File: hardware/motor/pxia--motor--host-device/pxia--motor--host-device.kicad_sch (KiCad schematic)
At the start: 5 parts

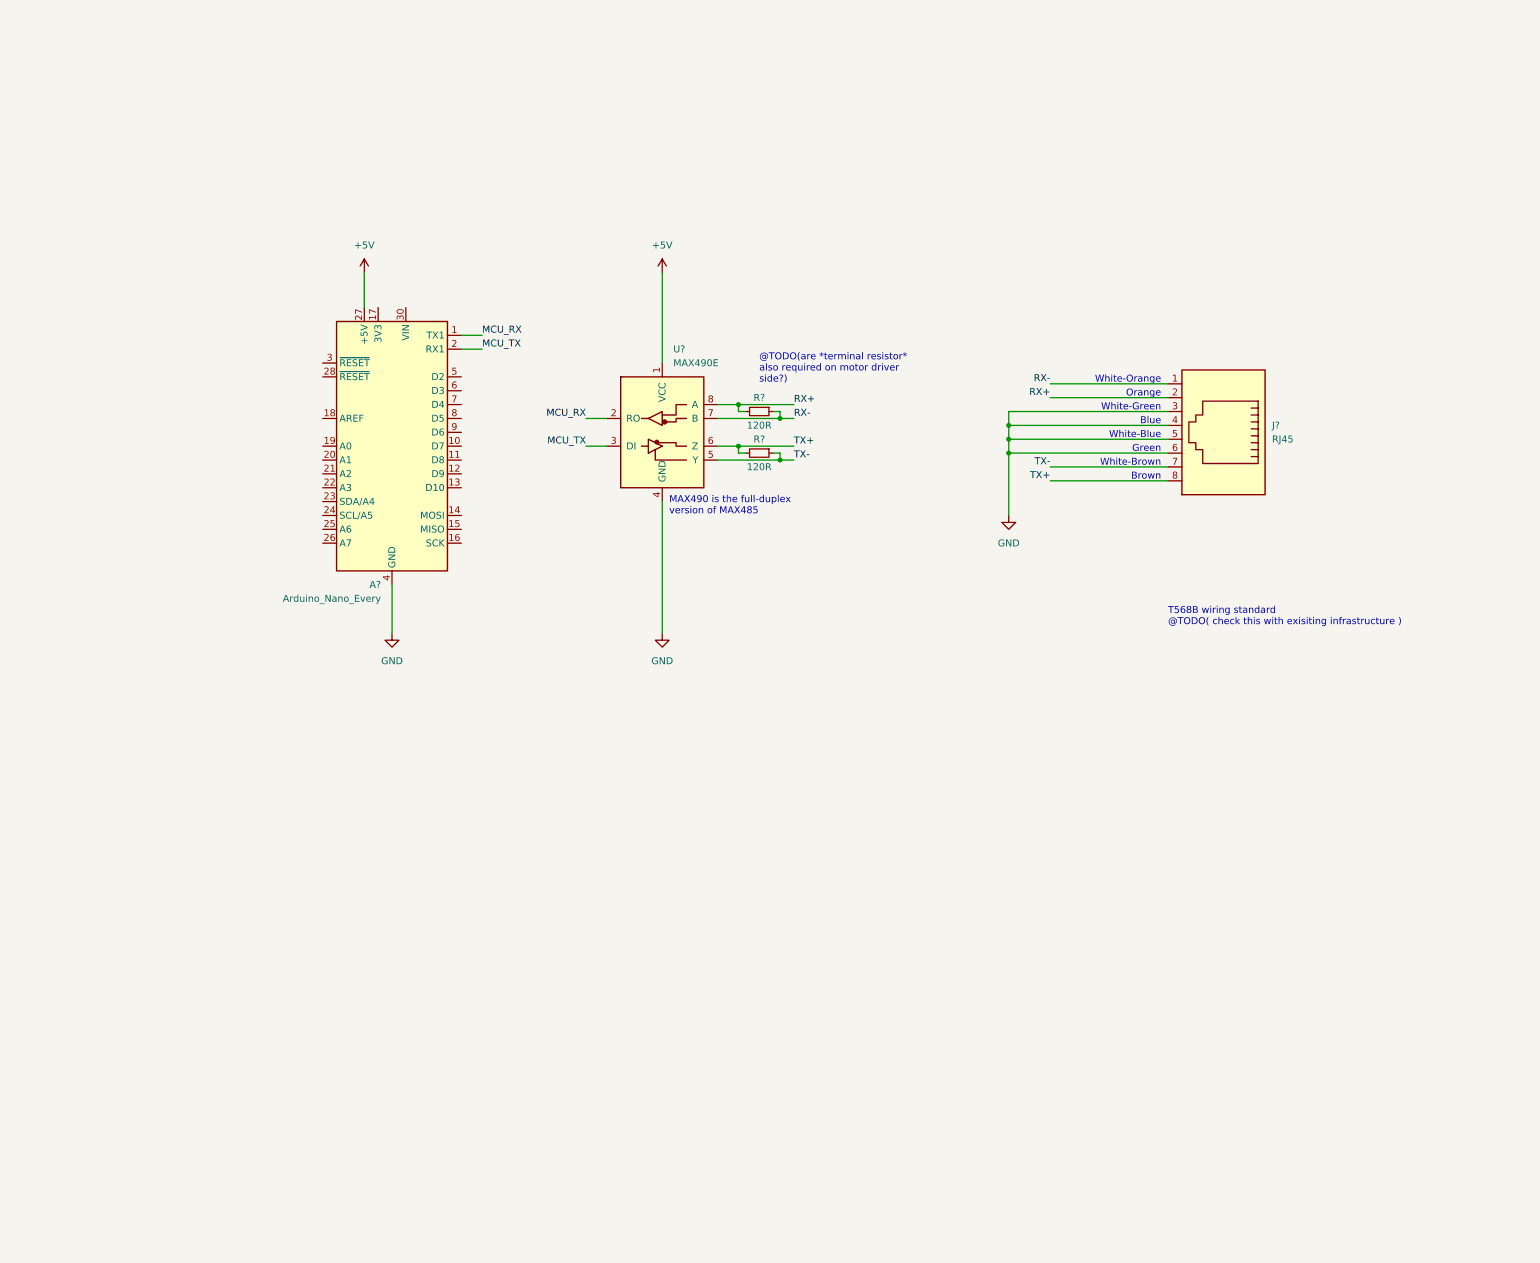
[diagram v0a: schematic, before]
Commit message: updated schematics + footprint
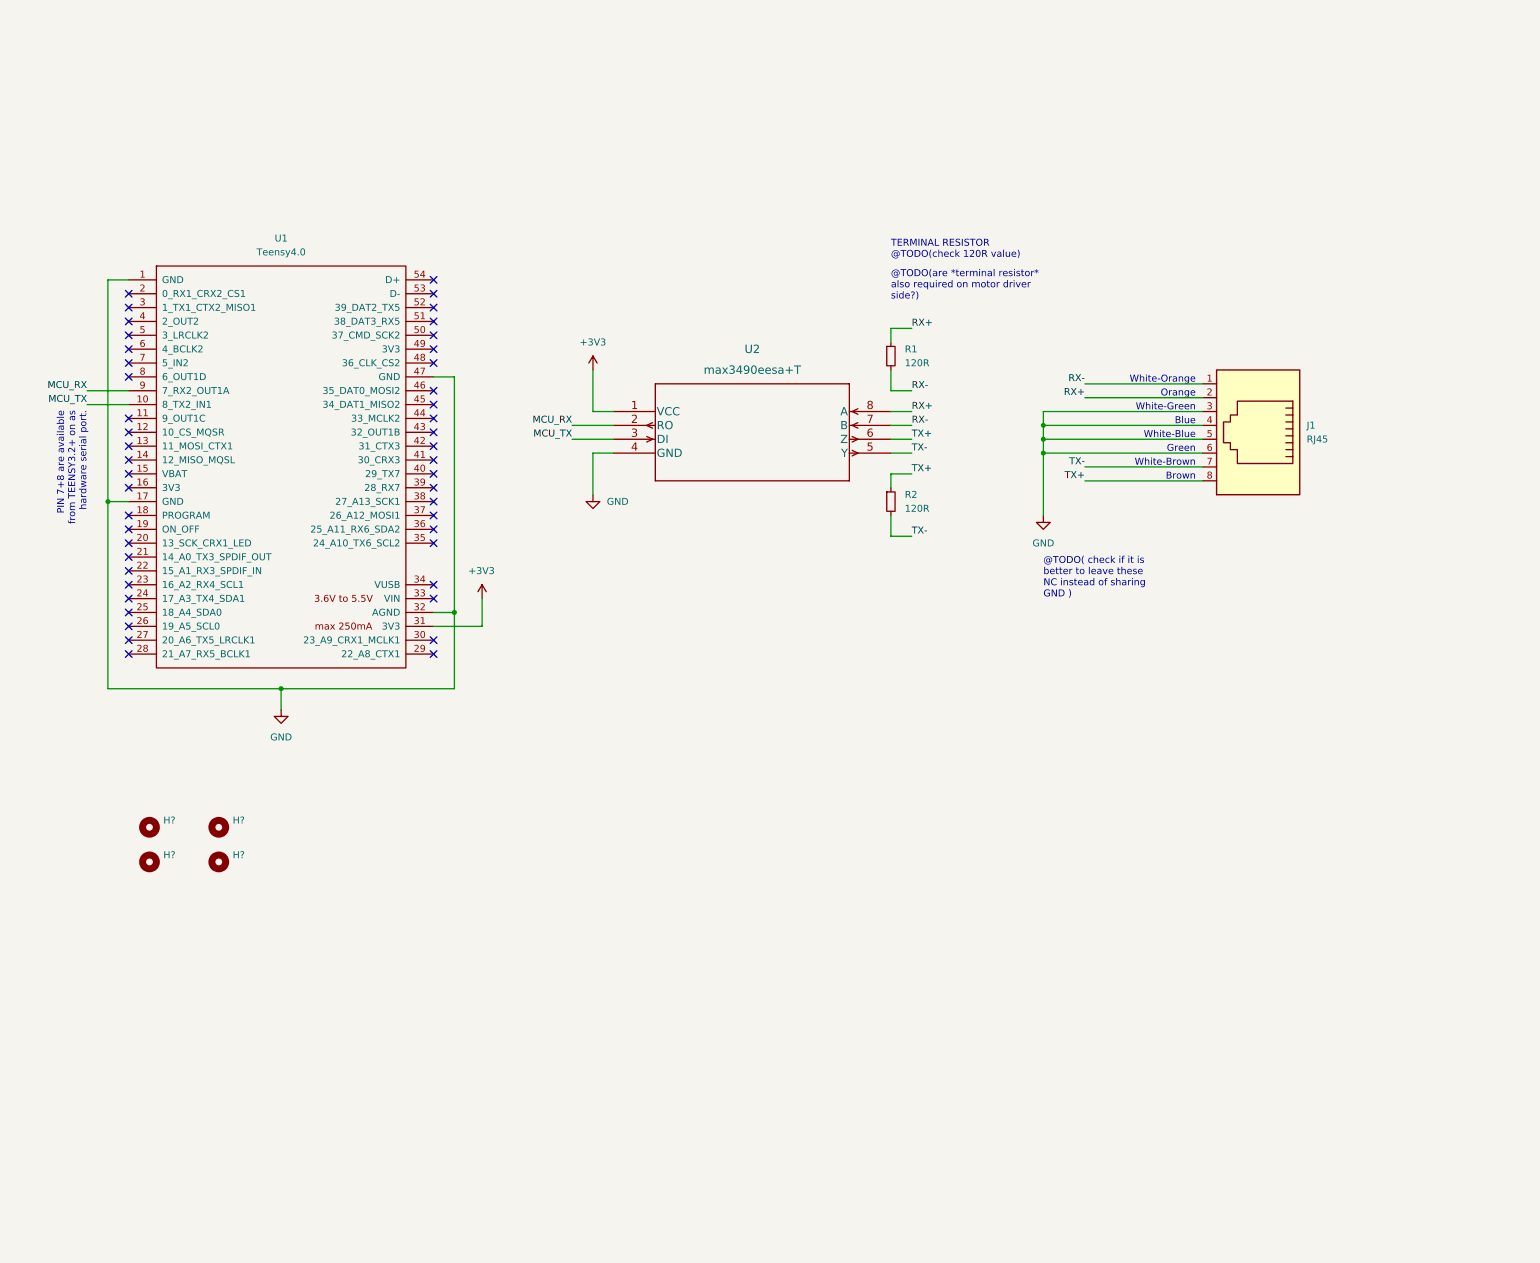
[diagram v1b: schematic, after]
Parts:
- removed A?: Arduino_Nano_Every, Module:Arduino_Nano, symbol MCU_Module:Arduino_Nano_Every
- removed R? (x2): 120R, symbol Device:R_Small
- removed U?: MAX490E, symbol Interface_UART:MAX490E
- added H? (x4): (no value), symbol Mechanical:MountingHole
- added R1, R2: 120R, Resistor_SMD:R_0805_2012Metric_Pad1.20x1.40mm_HandSolder, symbol Device:R_Small
- added U1: Teensy4.0, TEENSY:Teensy40, symbol teensy:Teensy4.0
- added U2: max3490eesa+T, Package_SO:SOIC-8_3.9x4.9mm_P1.27mm, symbol MAX3490EESA+T:max3490eesa+T
- J1: renamed from J?; footprint (none) -> Connector_RJ:RJ45_OST_PJ012-8P8CX_Vertical
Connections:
- net GND: now also U1.1 (GND), U1.17 (GND), U1.32 (AGND), U1.47 (GND), U2.4 (GND)
- net MCU_RX: now also U1.9 (7_RX2_OUT1A), U2.2 (RO)
- net MCU_TX: now also U1.10 (8_TX2_IN1), U2.3 (DI)
- net RX+: now also R1.1, U2.8 (A)
- net RX-: now also R1.2, U2.7 (B)
- net TX+: now also R2.1, U2.6 (Z)
- net TX-: now also R2.2, U2.5 (Y)
- new net +3V3: U1.31 (3V3), U2.1 (VCC)
- no-connect marks 0 -> 47
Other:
- note added: "@TODO( check if it is better to leave these NC instead of sharing GND )"
- note added: "PIN 7+8 are available from TEENSY3.2+ on as hardware serial port."
- note added: "TERMINAL RESISTOR @TODO(check 120R value)"
- note removed: "MAX490 is the full-duplex version of MAX485"
- note removed: "T568B wiring standard @TODO( check this with exisiting infrastructure )"
- moved on the sheet: J1

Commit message: added drawing, added ESP32 to host board
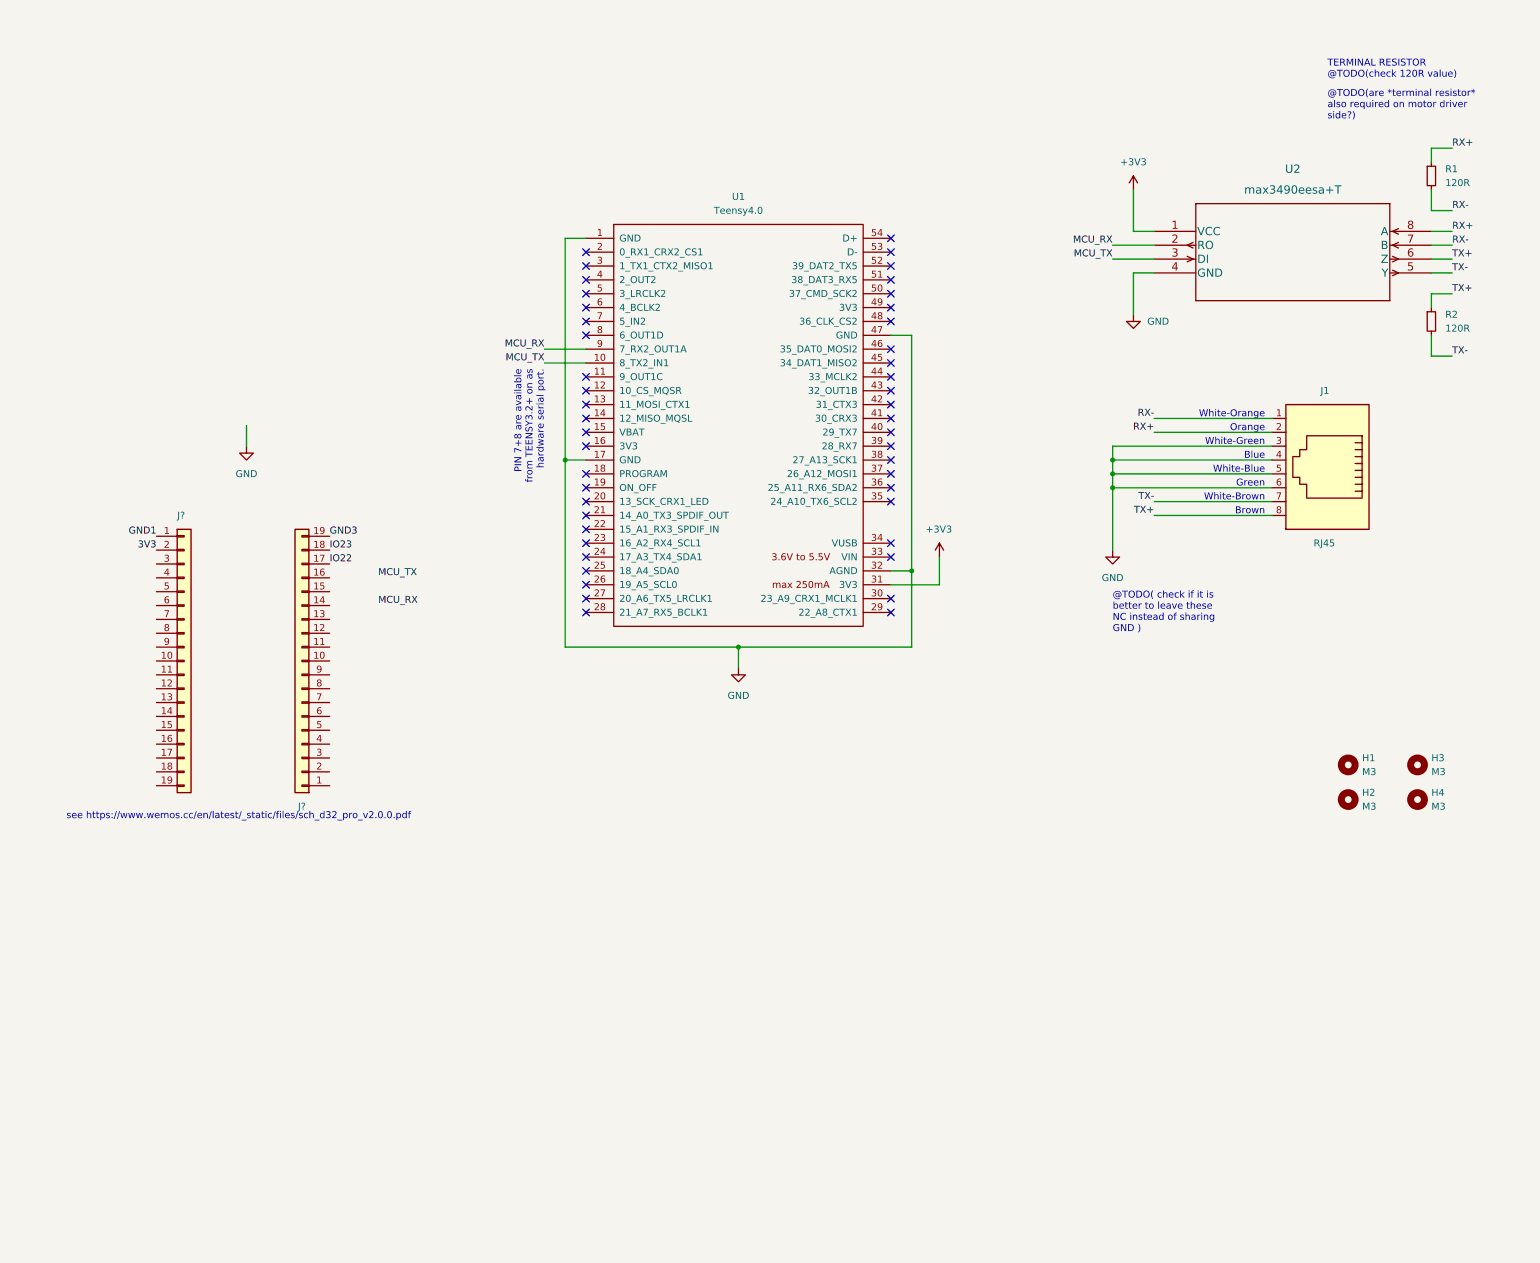
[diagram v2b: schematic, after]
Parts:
- added J? (x2): (no value), symbol Connector_Generic:Conn_01x19
- H1, H2, H3, H4: renamed from H?; value (none) -> M3; footprint (none) -> MountingHole:MountingHole_3.2mm_M3
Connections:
- new net 3V3: J?.2 (Pin_2)
- new net GND1: J?.1 (Pin_1)
- new net GND3: J?.19 (Pin_19)
- new net IO22: J?.17 (Pin_17)
- new net IO23: J?.18 (Pin_18)
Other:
- note added: "see https://www.wemos.cc/en/latest/_static/files/sch_d32_pro_v2.0.0.pdf"
- moved on the sheet: H1, H2, H3, H4, J1, R1, R2, U1, U2

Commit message: finished schematics and most of pcb layout
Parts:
- removed J? (x2): (no value), symbol Connector_Generic:Conn_01x19
- added J2: Lolin D32 Pro 2.0.0 (ESP32) PIN01–16, Connector_PinSocket_2.54mm:PinSocket_1x16_P2.54mm_Vertical, symbol Connector_Generic:Conn_01x16
- added J3: GENERIC_UART, Connector_Molex:Molex_Nano-Fit_105313-xx04_1x04_P2.50mm_Horizontal, symbol Connector_Generic:Conn_01x04
- added J4: Lolin D32 Pro 2.0.0 (ESP32) PIN17–32, Connector_PinSocket_2.54mm:PinSocket_1x16_P2.54mm_Vertical, symbol Connector_Generic:Conn_01x16
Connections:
- net +3V3: now also J2.1 (Pin_1), J3.1 (Pin_1)
- net GND: now also J3.4 (Pin_4), J4.1 (Pin_1), J4.16 (Pin_16); no longer J1.3, J1.4, J1.5, J1.6
- net MCU_RX renamed IO13
- net IO13: now also J2.13 (Pin_13), J3.3 (Pin_3)
- net MCU_TX renamed IO14/T-CS
- net IO14/T-CS: now also J2.11 (Pin_11), J3.2 (Pin_2)
- new net: J1.3, J1.4, J1.5, J1.6
- new net BAT: J2.16 (Pin_16)
- new net EN: J2.14 (Pin_14)
- new net IO00: J4.13 (Pin_13)
- new net IO02: J4.14 (Pin_14)
- new net IO04/TF-CS: J4.12 (Pin_12)
- new net IO05/SS: J4.9 (Pin_9)
- new net IO12/TS-CS: J2.12 (Pin_12)
- new net IO15: J4.15 (Pin_15)
- new net IO18/SCK: J4.8 (Pin_8)
- new net IO19/MISO: J4.7 (Pin_7)
- new net IO21/SDA: J4.6 (Pin_6)
- new net IO22/SCL: J4.3 (Pin_3)
- new net IO23/MOSI: J4.2 (Pin_2)
- new net IO25/DAC1: J2.8 (Pin_8)
- new net IO26/DAC2: J2.9 (Pin_9)
- new net IO27/T-DC: J2.10 (Pin_10)
- new net IO32/A/T-LED: J2.6 (Pin_6)
- new net IO33/A/T-RST: J2.7 (Pin_7)
- new net IO34/A: J2.5 (Pin_5)
- new net NC: J4.10 (Pin_10), J4.11 (Pin_11)
- new net RESET: J2.2 (Pin_2)
- new net RXD0: J4.5 (Pin_5)
- new net TXD0: J4.4 (Pin_4)
- new net USB: J2.15 (Pin_15)
- new net VN: J2.4 (Pin_4)
- new net VP: J2.3 (Pin_3)
- no-connect marks 47 -> 73
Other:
- note added: "@add https://shop.pimoroni.com/products/feathers3-esp32-s3?variant=39762596298835"
- note added: "@add https://shop.pimoroni.com/products/tiny-2040?variant=39560012234835"
- note added: "ETHERNET via: - Teensy 4.1 via Ethernet Kit for Teensy 4.1 https://www.pjrc.com/store/ethernet_kit.html - ESP32 via ESP32 Adafruit Ethernet FeatherWing https://shop.pimoroni.com/products/adafruit-ethernet-featherwing?variant=27079000007 - Tiny 2040 ??? - RPI Pico via WIZnet Ethernet HAT https://shop.pimoroni.com/products/wiznet-ethernet-hat?variant=39530105634899"
- note added: "Generic UART"
- note added: "HOST FOR: - ESP32 Feather https://shop.pimoroni.com/products/feathers2-esp32-s2?variant=32316476784723 - Teensy 3.2+ - Tiny 2040 - RPI Pico"
- note added: "LOLIN D32 Pro ESP32"
- note added: "MFR.Part # 5555799-1"
- note added: "MFR.Part # MAX3490EESA+T"
- note added: "RJ45"
- note added: "TEENSY3.2++"
- note added: "TTL–RS485"
- note added: "see https://www.wemos.cc/en/latest/d32/d32_pro.html"
- note removed: "@TODO( check if it is better to leave these NC instead of sharing GND )"
- note removed: "see https://www.wemos.cc/en/latest/_static/files/sch_d32_pro_v2.0.0.pdf"
- moved on the sheet: H1, H2, H3, H4, J1, R1, R2, U1, U2
